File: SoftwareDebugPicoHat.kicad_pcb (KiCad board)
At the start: 4 copper layers, 69 x 54.7 mm, 14 parts, among them J1 35362-0950, J2 Conn_Coaxial, J3 USB_C_Receptacle_USB2.0_14P, J4 Conn_Coaxial, J5 Conn_01x04_Pin, U1 RFM98PW, U3 LORA1280F27-TCXO

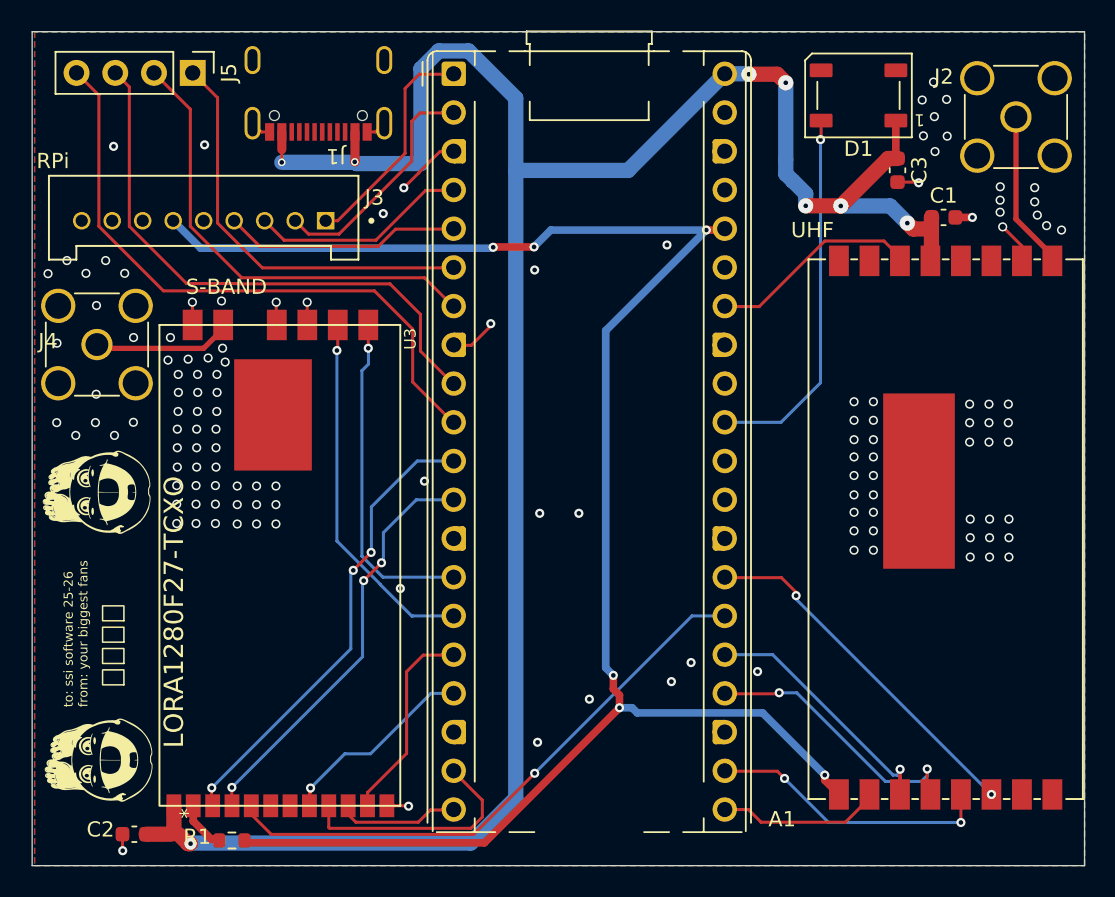
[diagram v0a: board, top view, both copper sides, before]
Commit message: Removed UBC and TCXO-EN Pullup resistor
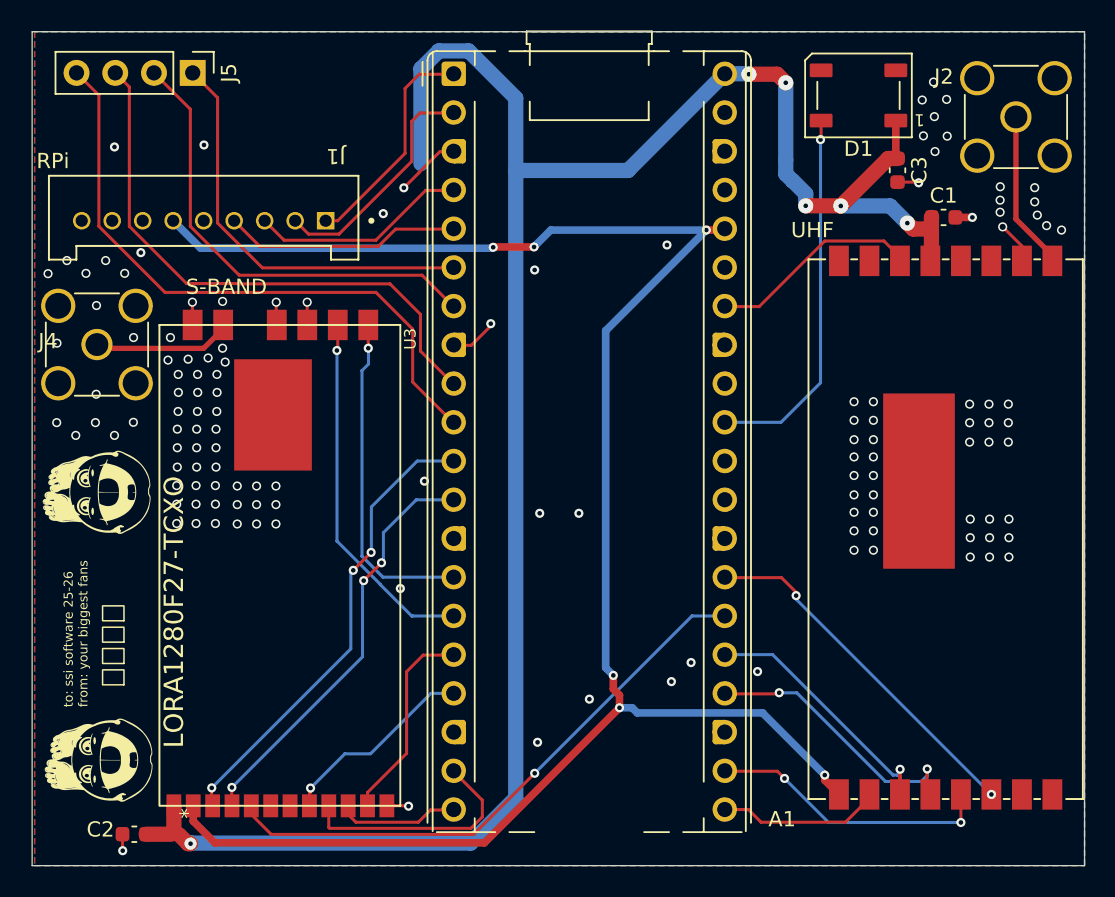
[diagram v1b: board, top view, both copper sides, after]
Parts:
- removed J3: USB_C_Receptacle_USB2.0_14P, ssi_connector:USB_C_Receptacle_XKB_U262-161N-4BVC11
- removed R1: 10k, Resistor_SMD:R_0603_1608Metric
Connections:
- U3 pad 2: SBAND_TCXOEN -> +3V3
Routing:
- net +5V: track 149.4 -> 136.2 mm, vias 8 -> 6
- net +3V3: track 117.4 -> 122.2 mm
- net SBAND_TCXOEN: track 3.22 -> 0.00 mm
- net GND: track 22.4 -> 19.7 mm, vias 132 -> 133

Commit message: FIxed Caps
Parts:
- added C4: 10uf, Capacitor_SMD:C_0603_1608Metric, F.Cu at (129.8, 105.9)
- moved C2 1.37 mm to (129.9, 104.0)
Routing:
- net +5V: track 136.2 -> 120.3 mm
- net GND: track 19.7 -> 20.3 mm, vias 133 -> 134
